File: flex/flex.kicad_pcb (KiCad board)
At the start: 2 copper layers, 104.1 x 90.6 mm, 105 parts, among them J1 Conn_01x04_Female, J2 Conn_01x05_Female, J3 Conn_01x03_Female, J4 Conn_01x06_Female, J5 Conn_01x03_Female, SW10 NA_SW_Push, SW11 NA_SW_Push, SW12 NA_SW_Push, SW15 NA_SW_Push, SW16 NA_SW_Push, SW17 NA_SW_Push, SW20 NA_SW_Push, SW21 NA_SW_Push, SW22 NA_SW_Push, SW24 NA_SW_Push, SW25 NA_SW_Push, SW26 NA_SW_Push, SW6 NA_SW_Push, SW7 NA_SW_Push, SW8 NA_SW_Push

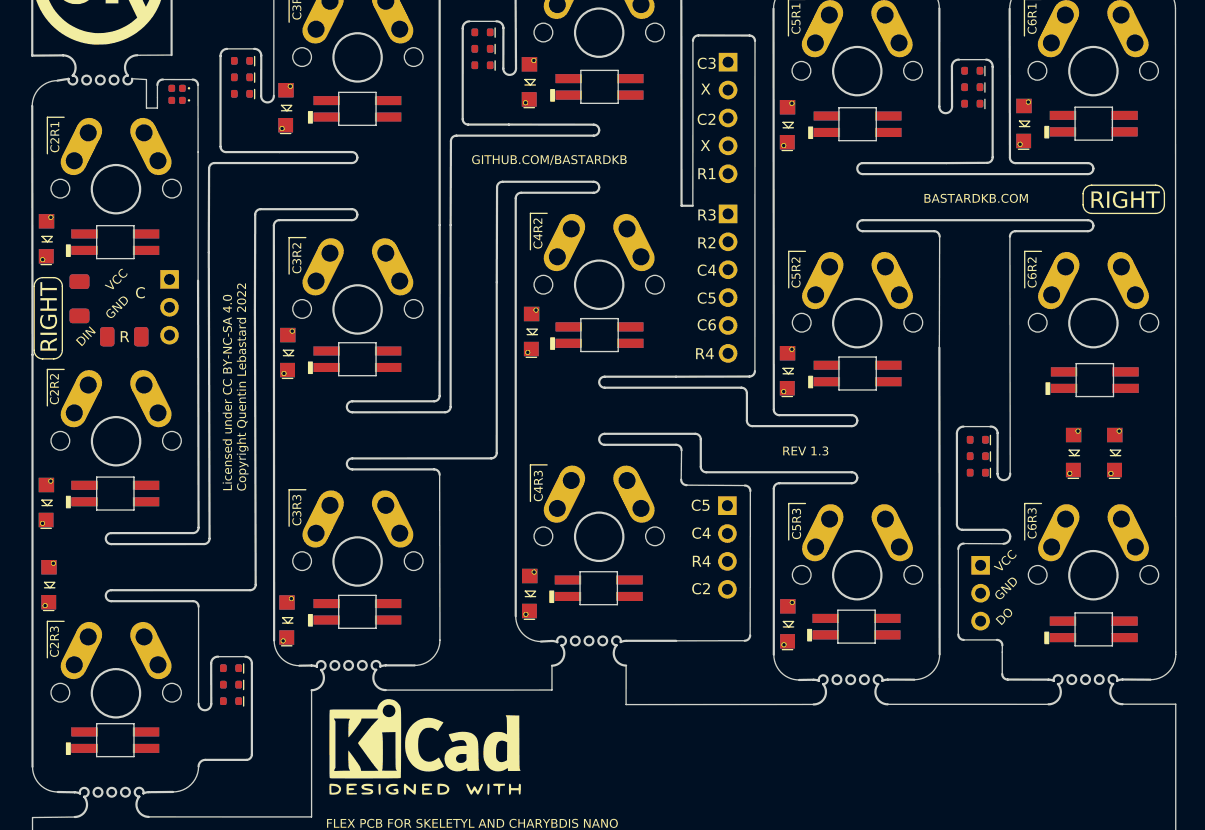
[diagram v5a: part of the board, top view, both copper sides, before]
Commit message: change LEDs
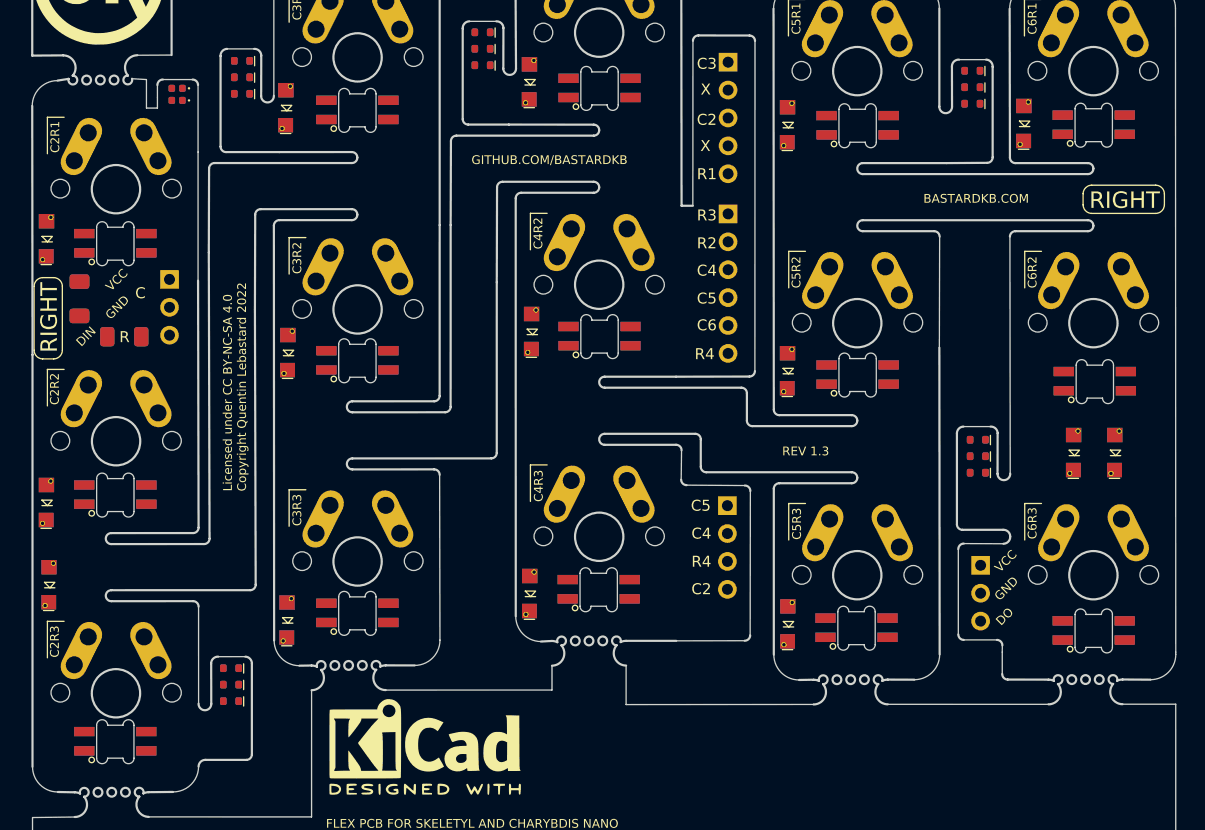
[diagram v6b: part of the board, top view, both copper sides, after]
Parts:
- D21, D23, D25, D33, D37, D39, D41, D47, D49, D5, D51, D55, D57, D59, D7: value SK6812MINI -> RIGHT_LED; footprint libs2:YS-SK6812MINI-E_REVERSE -> custom:SK6812_mini_e_corners
- D22, D24, D26, D34, D38, D40, D42, D48, D50, D52, D56, D58, D6, D60, D8: value SK6812MINI -> LEFT_LED; footprint libs2:YS-SK6812MINI-E_REVERSE_NO_EDGECUT -> custom:SK6812_mini_e_corners_noedgecuts
- moved D6 0.19 mm to (65.2, 128.6)
- moved D8 0.19 mm to (65.2, 106.2)
- moved D22 0.19 mm to (87.2, 71.2)
- moved D24 0.19 mm to (87.2, 94.0)
- moved D26 0.19 mm to (87.2, 117.0)
- moved D34 0.19 mm to (65.2, 83.3)
- moved D38 0.19 mm to (109.2, 114.8)
- moved D48 0.19 mm to (132.8, 72.6)
- moved D52 0.19 mm to (132.7, 118.3)
- moved D58 0.19 mm to (154.4, 95.9)
- moved D40 0.19 mm to (109.3, 91.8)
- moved D42 0.19 mm to (109.3, 69.2)
- moved D50 0.19 mm to (132.8, 95.3)
- moved D56 0.19 mm to (154.3, 72.5)
- moved D60 0.19 mm to (154.3, 118.6)
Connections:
- D21 pad 2: Net-(D21-VSS) -> Gnd
- D21 pad 4: Net-(D21-VDD) -> Vcc
- D22 pad 2: Net-(D22-VSS) -> Gnd
- D22 pad 4: Net-(D22-VDD) -> Vcc
- D23 pad 2: Net-(D21-VSS) -> Gnd
- D23 pad 4: Net-(D21-VDD) -> Vcc
- D24 pad 2: Net-(D22-VSS) -> Gnd
- D24 pad 4: Net-(D22-VDD) -> Vcc
- D25 pad 2: Net-(D21-VSS) -> Gnd
- D25 pad 4: Net-(D21-VDD) -> Vcc
- D26 pad 2: Net-(D22-VSS) -> Gnd
- D26 pad 4: Net-(D22-VDD) -> Vcc
- D33 pad 4: Net-(D33-VDD) -> Vcc
- D34 pad 1: unconnected-(D34-DOUT-Pad1) -> Net-(D21-DIN)
- D37 pad 2: Net-(D21-VSS) -> Gnd
- D37 pad 4: Net-(D21-VDD) -> Vcc
- D38 pad 2: Net-(D22-VSS) -> Gnd
- D38 pad 4: Net-(D22-VDD) -> Vcc
- D39 pad 2: Net-(D21-VSS) -> Gnd
- D39 pad 4: Net-(D21-VDD) -> Vcc
- D40 pad 2: Net-(D22-VSS) -> Gnd
- D40 pad 4: Net-(D22-VDD) -> Vcc
- D41 pad 2: Net-(D21-VSS) -> Gnd
- D41 pad 4: Net-(D21-VDD) -> Vcc
- D42 pad 2: Net-(D22-VSS) -> Gnd
- D42 pad 4: Net-(D22-VDD) -> Vcc
- D47 pad 2: Net-(D21-VSS) -> Gnd
- D47 pad 4: Net-(D47-VDD) -> Vcc
- D48 pad 2: Net-(D48-VSS) -> Gnd
- D48 pad 4: Net-(D48-VDD) -> Vcc
- D49 pad 2: Net-(D21-VSS) -> Gnd
- D49 pad 4: Net-(D47-VDD) -> Vcc
- D5 pad 4: Net-(D33-VDD) -> Vcc
- D50 pad 2: Net-(D48-VSS) -> Gnd
- D50 pad 4: Net-(D48-VDD) -> Vcc
- D51 pad 2: Net-(D21-VSS) -> Gnd
- D51 pad 4: Net-(D47-VDD) -> Vcc
- D52 pad 2: Net-(D48-VSS) -> Gnd
- D52 pad 4: Net-(D48-VDD) -> Vcc
- D55 pad 2: Net-(D55-VSS) -> Gnd
- D55 pad 4: Net-(D47-VDD) -> Vcc
- D56 pad 2: Net-(D48-VSS) -> Gnd
- D56 pad 4: Net-(D48-VDD) -> Vcc
- D57 pad 2: Net-(D55-VSS) -> Gnd
- D57 pad 4: Net-(D47-VDD) -> Vcc
- D58 pad 2: Net-(D48-VSS) -> Gnd
- D58 pad 4: Net-(D48-VDD) -> Vcc
- D59 pad 2: Net-(D55-VSS) -> Gnd
- D59 pad 4: Net-(D47-VDD) -> Vcc
- D60 pad 2: Net-(D48-VSS) -> Gnd
- D60 pad 4: Net-(D48-VDD) -> Vcc
- D7 pad 4: Net-(D33-VDD) -> Vcc
- R1 pad 2: Net-(R1-Pad2) -> Net-(D5-DIN)
- R2 pad 2: Net-(R1-Pad2) -> Net-(D5-DIN)
- R3 pad 2: Net-(R1-Pad2) -> Net-(D5-DIN)
